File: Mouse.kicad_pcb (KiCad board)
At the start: 2 copper layers, 28 x 9.8 mm, 27 parts, among them J1 Conn_01x05_Male, U1 Left click, U2 Middle click, U3 Right Click, U4 LQ1, U5 Optical_Sensor

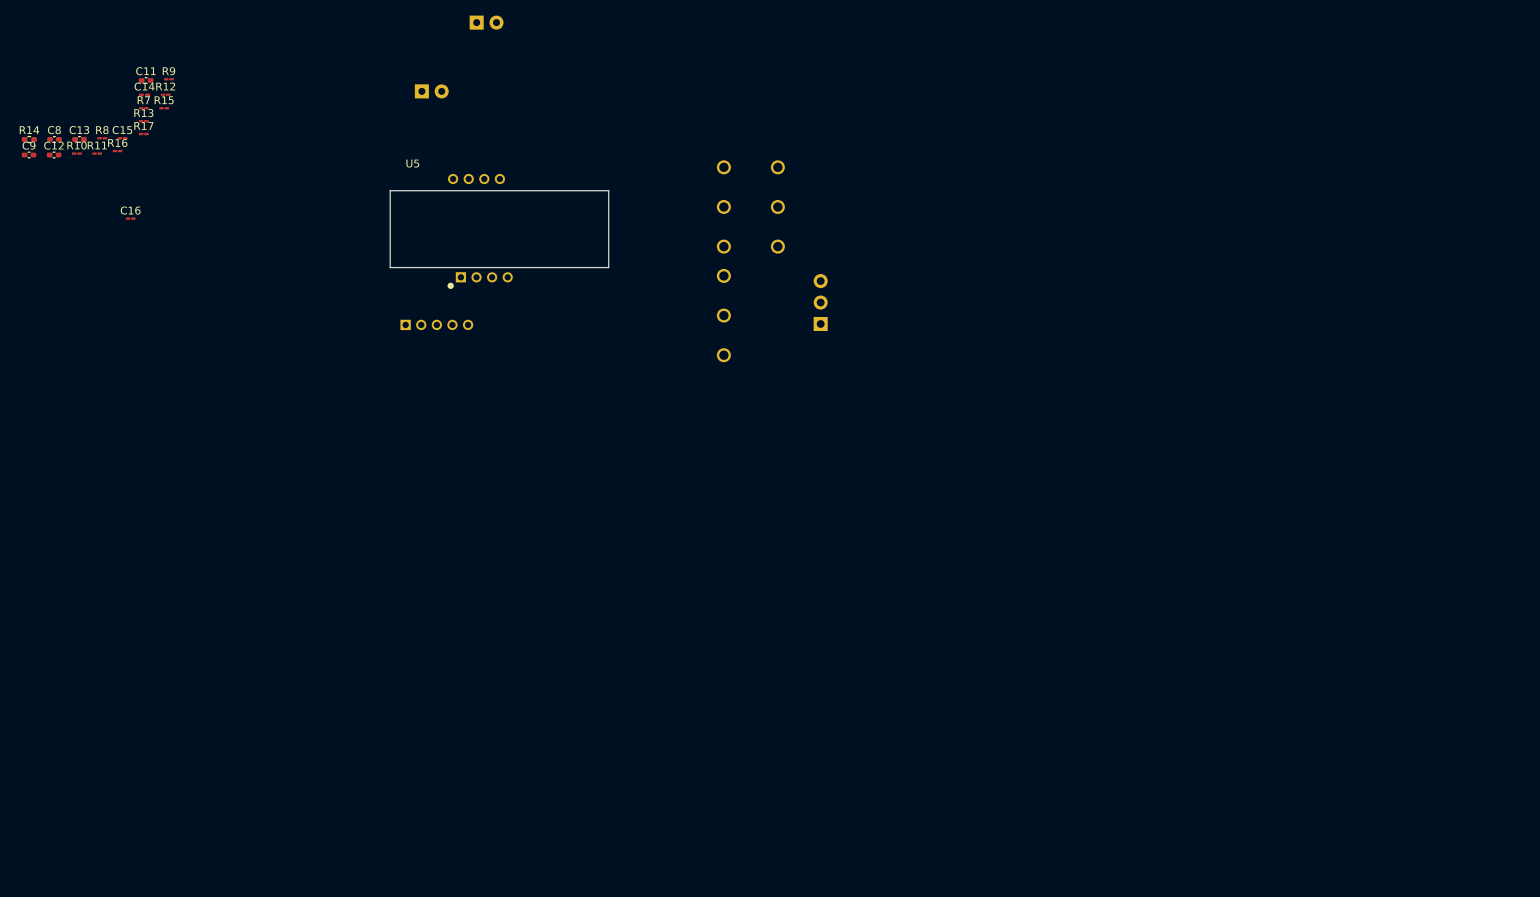
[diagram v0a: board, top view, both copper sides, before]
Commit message: created the inner and outer edge cuts
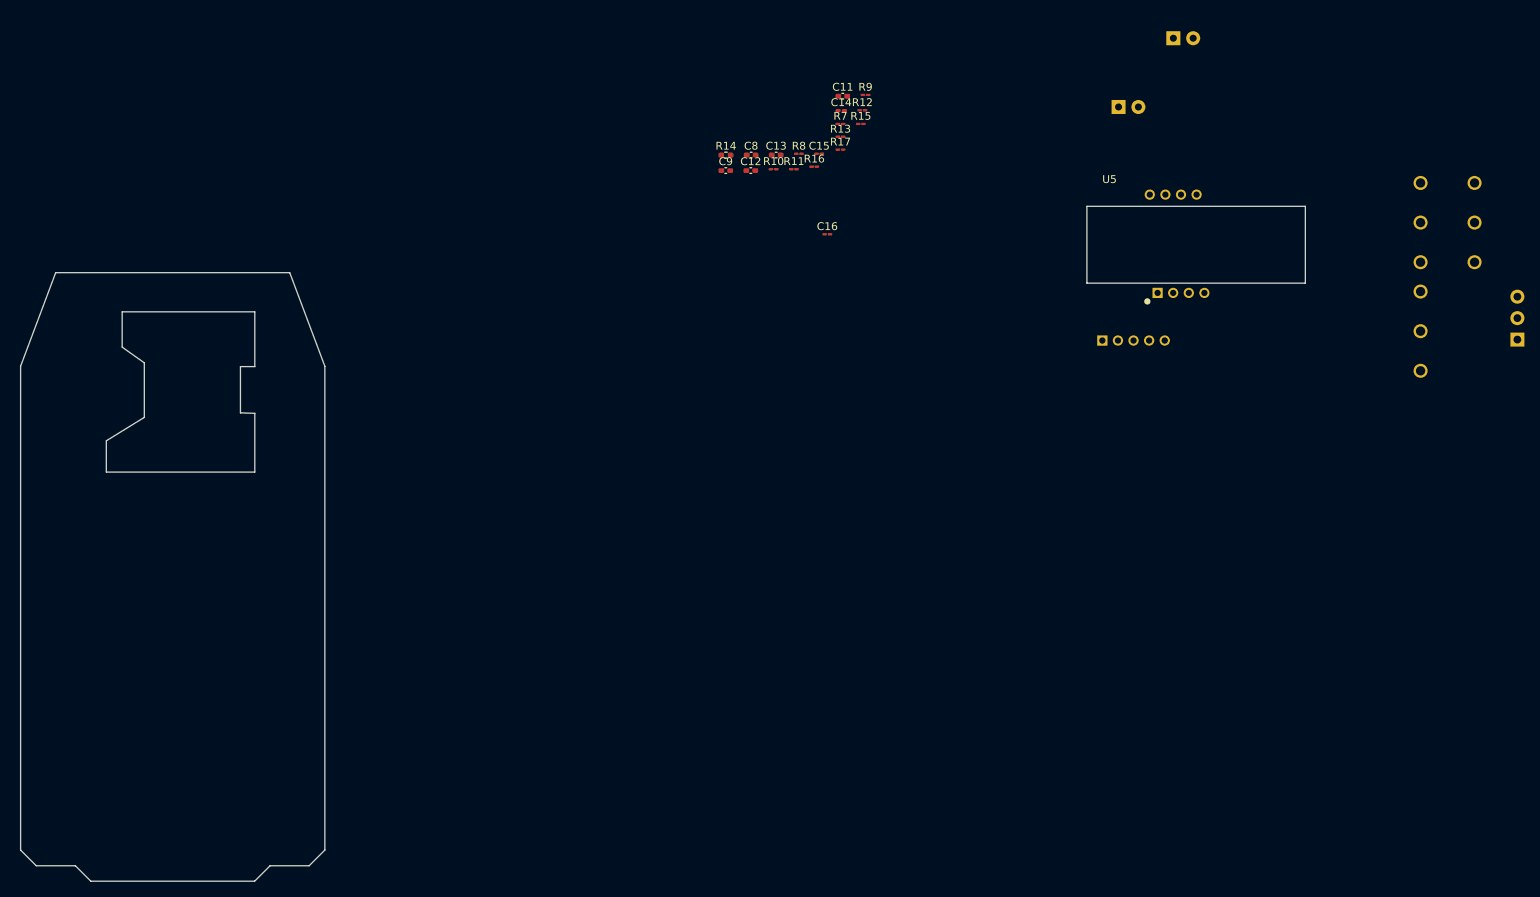
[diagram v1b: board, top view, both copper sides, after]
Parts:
- moved U3 89.3 mm to (263.5, 68.4)
- moved J1 89.3 mm to (219.8, 83.5)
- moved R12 89.3 mm to (185.0, 54.0)
- moved R9 89.3 mm to (185.4, 52.1)
- moved U1 89.3 mm to (256.6, 68.4)
- moved U2 89.3 mm to (256.6, 82.3)
- moved C12 89.3 mm to (170.7, 61.8)
- moved C13 89.3 mm to (174.0, 59.8)
- moved C14 89.3 mm to (182.3, 54.1)
- moved C15 89.3 mm to (179.5, 59.6)
- moved C16 89.3 mm to (180.6, 69.9)
- moved R10 89.3 mm to (173.7, 61.6)
- moved R11 89.3 mm to (176.3, 61.6)
- moved R13 89.3 mm to (182.2, 57.4)
- moved R14 89.3 mm to (167.6, 59.8)
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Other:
- board size 28 x 9.8 mm -> 39 x 78 mm

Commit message: updated footprints
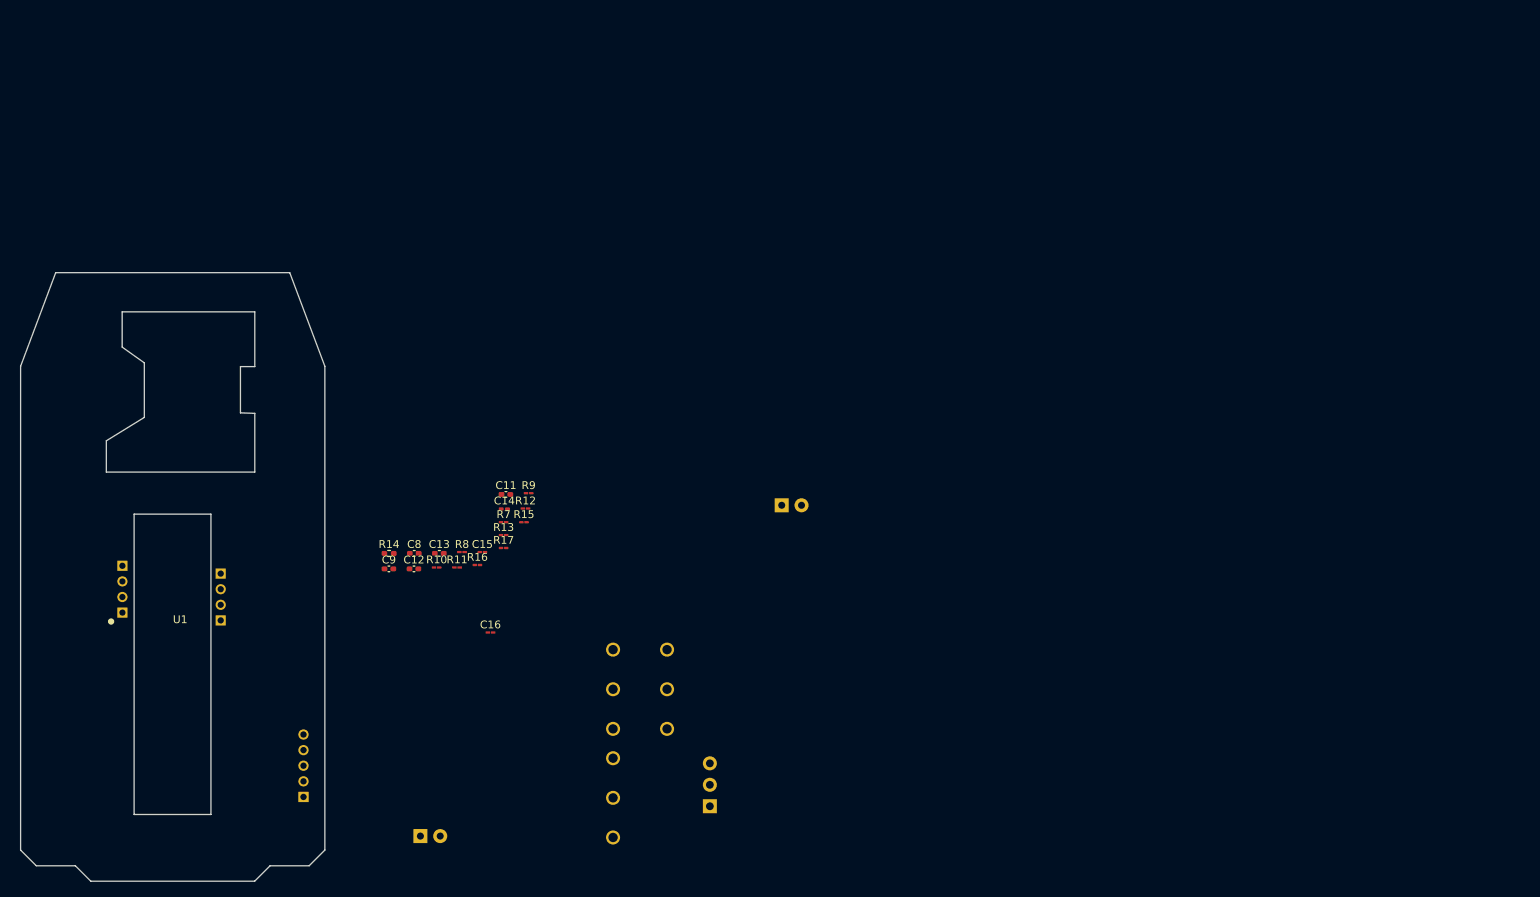
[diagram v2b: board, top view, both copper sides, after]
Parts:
- U5: moved to B.Cu
- moved LD2 140.6 mm to (128.4, 147.1)
- moved U5 131.8 mm to (96.5, 115.0), turned to 270 degrees
- moved U2 119.5 mm to (153.1, 142.2)
- moved U1 119.5 mm to (153.1, 128.2)
- moved U3 119.5 mm to (160.0, 128.2)
- moved U4 119.5 mm to (165.5, 140.5)
- moved J1 119.5 mm to (113.4, 138.0), turned to 90 degrees
- moved C13 66.9 mm to (130.8, 110.8)
- moved C14 66.9 mm to (139.2, 105.1)
- moved C15 66.9 mm to (136.3, 110.7)
- moved C16 66.9 mm to (137.4, 121.0)
- moved R11 66.9 mm to (133.1, 112.6)
- moved R12 66.9 mm to (141.9, 105.1)
- moved R17 66.9 mm to (139.1, 110.1)
- moved R7 66.9 mm to (139.1, 106.8)
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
